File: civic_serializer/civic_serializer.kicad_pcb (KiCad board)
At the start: 2 copper layers, 65 x 30 mm, 5 parts, among them J1 GPIO

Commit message: - done some of the layout
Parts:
- added C1: 100n, Capacitor_SMD:C_0805_2012Metric_Pad1.18x1.45mm_HandSolder, F.Cu at (58.6, 45.9)
- added C10: 4.7u, Capacitor_SMD:C_0805_2012Metric_Pad1.18x1.45mm_HandSolder, F.Cu at (63.4, 57.9)
- added C11: 100n, Capacitor_SMD:C_0805_2012Metric_Pad1.18x1.45mm_HandSolder, F.Cu at (153.3, 83.7)
- added C12: 100n, Capacitor_SMD:C_0805_2012Metric_Pad1.18x1.45mm_HandSolder, F.Cu at (153.3, 86.5)
- added C13: 10uF, Capacitor_SMD:C_0805_2012Metric_Pad1.18x1.45mm_HandSolder, F.Cu at (68.2, 51.9)
- added C2: 10u, Capacitor_SMD:C_0805_2012Metric_Pad1.18x1.45mm_HandSolder, F.Cu at (58.6, 48.9)
- added C3: 10u, Capacitor_SMD:C_0805_2012Metric_Pad1.18x1.45mm_HandSolder, F.Cu at (58.6, 51.9)
- added C4: 10u, Capacitor_SMD:C_0805_2012Metric_Pad1.18x1.45mm_HandSolder, F.Cu at (58.6, 54.9)
- added C5: 4.7u, Capacitor_SMD:C_0805_2012Metric_Pad1.18x1.45mm_HandSolder, F.Cu at (58.6, 57.9)
- added C6: 4.7u, Capacitor_SMD:C_0805_2012Metric_Pad1.18x1.45mm_HandSolder, F.Cu at (63.4, 45.9)
- added C7: 4.7u, Capacitor_SMD:C_0805_2012Metric_Pad1.18x1.45mm_HandSolder, F.Cu at (63.4, 48.9)
- added C8: 4.7u, Capacitor_SMD:C_0805_2012Metric_Pad1.18x1.45mm_HandSolder, F.Cu at (63.4, 51.9)
- added C9: 4.7u, Capacitor_SMD:C_0805_2012Metric_Pad1.18x1.45mm_HandSolder, F.Cu at (63.4, 54.9)
- added D1: LED, LED_SMD:LED_0805_2012Metric_Pad1.15x1.40mm_HandSolder, F.Cu at (68.1, 61.0)
- added FB1: FerriteBead, Inductor_SMD:L_0805_2012Metric_Pad1.05x1.20mm_HandSolder, F.Cu at (63.2, 60.8)
- added FB2: FerriteBead, Inductor_SMD:L_0805_2012Metric_Pad1.05x1.20mm_HandSolder, F.Cu at (63.2, 63.6)
- added I2C1: Conn_01x02_Socket, Connector_PinSocket_2.54mm:PinSocket_1x02_P2.54mm_Vertical, F.Cu at (144.4, 97.0)
- added IC1: DS90UB925QSQX_NOPB, Footprint_library:QFN50P700X700X80-49N-D, F.Cu at (144.7, 85.6)
- added LVDS1: Conn_01x03_Pin, Connector_JST:JST_NV_B03P-NV_1x03_P5.00mm_Vertical, F.Cu at (159.4, 89.9)
- added R1: 4K7, Resistor_SMD:R_0805_2012Metric_Pad1.20x1.40mm_HandSolder, F.Cu at (53.8, 35.3)
- added R2: 10K, Resistor_SMD:R_0805_2012Metric_Pad1.20x1.40mm_HandSolder, F.Cu at (53.8, 38.3)
- added R3: 4K7, Resistor_SMD:R_0805_2012Metric_Pad1.20x1.40mm_HandSolder, F.Cu at (53.8, 41.2)
- added R4: 4K7, Resistor_SMD:R_0805_2012Metric_Pad1.20x1.40mm_HandSolder, F.Cu at (53.8, 44.2)
- added R5: 4K7, Resistor_SMD:R_0805_2012Metric_Pad1.20x1.40mm_HandSolder, F.Cu at (53.8, 47.1)
- added R6: 100R, Resistor_SMD:R_0805_2012Metric_Pad1.20x1.40mm_HandSolder, F.Cu at (53.8, 50.1)
- added R7: R, Resistor_SMD:R_0805_2012Metric_Pad1.20x1.40mm_HandSolder, F.Cu at (53.8, 53.0)
- added R8: 100R, Resistor_SMD:R_0805_2012Metric_Pad1.20x1.40mm_HandSolder, F.Cu at (53.8, 56.0)
- added R9: R, Resistor_SMD:R_0805_2012Metric_Pad1.20x1.40mm_HandSolder, F.Cu at (53.8, 58.9)
- added RV1: R_Potentiometer_Trim, Potentiometer_THT:Potentiometer_Vishay_T93YA_Vertical, F.Cu at (114.2, 93.4)
- added RV2: R_Potentiometer_Trim, Potentiometer_THT:Potentiometer_Vishay_T93YA_Vertical, F.Cu at (73.7, 54.7)
- added U1: AMS1117-3.3, Package_TO_SOT_SMD:SOT-223-3_TabPin2, F.Cu at (75.5, 62.2)
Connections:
- J1 pad 10: /GPIO15/RXD0 -> G3
- J1 pad 11: /GPIO17 -> G5
- J1 pad 12: /GPIO18/PCM.CLK -> G6
- J1 pad 13: /GPIO27 -> R7
- J1 pad 15: /GPIO22 -> R2
- J1 pad 16: /GPIO23 -> R3
- J1 pad 18: /GPIO24 -> R4
- J1 pad 19: /GPIO10/SPI0.MOSI -> B6
- J1 pad 21: /GPIO9/SPI0.MISO -> B5
- J1 pad 22: /GPIO25 -> R5
- J1 pad 23: /GPIO11/SPI0.SCLK -> B7
- J1 pad 24: /GPIO8/SPI0.CE0 -> B4
- J1 pad 26: /GPIO7/SPI0.CE1 -> B3
- J1 pad 27: /ID_SDA -> PCLK
- J1 pad 28: /ID_SCL -> DE
- J1 pad 29: /GPIO5 -> B1
- J1 pad 3: /GPIO2/SDA1 -> VSYNC
- J1 pad 31: /GPIO6 -> B2
- J1 pad 32: /GPIO12/PWM0 -> G0
- J1 pad 33: /GPIO13/PWM1 -> G1
- J1 pad 35: /GPIO19/PCM.FS -> G7
- J1 pad 36: /GPIO16 -> G4
- J1 pad 37: /GPIO26 -> R6
- J1 pad 38: /GPIO20/PCM.DIN -> R0
- J1 pad 40: /GPIO21/PCM.DOUT -> R1
- J1 pad 5: /GPIO3/SCL1 -> HSYNC
- J1 pad 7: /GPIO4/GPCLK0 -> B0
- J1 pad 8: /GPIO14/TXD0 -> G2
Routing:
- net B7: track 0.00 -> 41.0 mm, vias 0 -> 5
- net VSYNC: track 0.00 -> 40.3 mm
- net HSYNC: track 0.00 -> 36.9 mm
- net G3: track 0.00 -> 36.9 mm
- net G6: track 0.00 -> 31.9 mm, vias 0 -> 1
- net G2: track 0.00 -> 31.3 mm
- net B6: track 0.00 -> 30.1 mm, vias 0 -> 3
- net R3: track 0.00 -> 29.6 mm
- net B5: track 0.00 -> 27.9 mm, vias 0 -> 4
- net R2: track 0.00 -> 25.7 mm
- net R4: track 0.00 -> 25.6 mm, vias 0 -> 1
- net B4: track 0.00 -> 25.5 mm, vias 0 -> 2
- net G4: track 0.00 -> 25.5 mm, vias 0 -> 1
- net G7: track 0.00 -> 25.5 mm, vias 0 -> 2
- net B3: track 0.00 -> 25.3 mm, vias 0 -> 2
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- added copper zone on B.Cu, net GND
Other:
- board text removed: "Extend PCB edge 0.5mm if using SMT header"
- board text removed: "PoE"

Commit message: - layout finished
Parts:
- removed D1: LED, LED_SMD:LED_0805_2012Metric_Pad1.15x1.40mm_HandSolder
- removed RV1, RV2: R_Potentiometer_Trim, Potentiometer_THT:Potentiometer_Vishay_T93YA_Vertical
- added 5V1: LED, LED_SMD:LED_0805_2012Metric_Pad1.15x1.40mm_HandSolder, F.Cu at (103.3, 79.4)
- added IDX1: R_Potentiometer_Trim, Potentiometer_THT:Potentiometer_Vishay_T93YA_Vertical, F.Cu at (117.9, 94.9)
- added IDX2: TestPoint, Connector_PinSocket_2.54mm:PinSocket_1x01_P2.54mm_Vertical, F.Cu at (111.4, 97.1)
- added MDE1: TestPoint, Connector_PinSocket_2.54mm:PinSocket_1x01_P2.54mm_Vertical, F.Cu at (132.9, 97.1)
- added MD_SEL1: R_Potentiometer_Trim, Potentiometer_THT:Potentiometer_Vishay_T93YA_Vertical, F.Cu at (126.3, 95.0)
- C1, C13: footprint Capacitor_SMD:C_0805_2012Metric_Pad1.18x1.45mm_HandSolder -> Capacitor_SMD:C_0603_1608Metric_Pad1.08x0.95mm_HandSolder; moved to B.Cu
- C10, C11, C12, C5, C6, C7, C8, C9: footprint Capacitor_SMD:C_0805_2012Metric_Pad1.18x1.45mm_HandSolder -> Capacitor_SMD:C_0603_1608Metric_Pad1.08x0.95mm_HandSolder
- C2, C3, C4: moved to B.Cu
- FB1, FB2: footprint Inductor_SMD:L_0805_2012Metric_Pad1.05x1.20mm_HandSolder -> Inductor_SMD:L_0603_1608Metric_Pad1.05x0.95mm_HandSolder; moved to B.Cu
- R2, R3, R4, R5: footprint Resistor_SMD:R_0805_2012Metric_Pad1.20x1.40mm_HandSolder -> Resistor_SMD:R_0603_1608Metric_Pad0.98x0.95mm_HandSolder; moved to B.Cu
- R6, R7, R8, R9: footprint Resistor_SMD:R_0805_2012Metric_Pad1.20x1.40mm_HandSolder -> Resistor_SMD:R_0603_1608Metric_Pad0.98x0.95mm_HandSolder
- moved R4 109.4 mm to (149.0, 98.0)
- moved R2 107.8 mm to (150.0, 86.9)
- moved R5 107.2 mm to (149.0, 96.4)
- moved C1 98.3 mm to (149.3, 83.9), turned to -90 degrees
- moved C7 95.7 mm to (149.9, 89.7)
- moved C8 94.9 mm to (149.0, 92.9)
- moved R3 94.7 mm to (139.8, 81.0), turned to 180 degrees
- moved C9 94.4 mm to (149.0, 94.5)
- moved C10 92.3 mm to (149.4, 91.3)
- moved C13 89.7 mm to (150.0, 88.6)
- moved C6 88.4 mm to (145.0, 79.9), turned to 180 degrees
- moved C5 83.7 mm to (139.1, 81.0)
- moved FB2 83.7 mm to (145.5, 78.9)
- moved FB1 78.7 mm to (139.8, 78.9)
- moved R7 78.5 mm to (125.4, 85.3), turned to 90 degrees
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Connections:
- net Net-(IC1-DOUT+) renamed DOUT+
- net Net-(IC1-DOUT-) renamed DOUT-
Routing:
- net VDDIO: track 0.00 -> 97.9 mm, vias 0 -> 6
- net GND: track 0.00 -> 81.0 mm, vias 8 -> 10
- net 3V3: track 0.00 -> 50.2 mm, vias 0 -> 2
- net MODE_SEL: track 0.00 -> 47.2 mm, vias 0 -> 1
- net DE: track 0.63 -> 44.9 mm, vias 0 -> 4
- net IDX: track 0.00 -> 43.7 mm, vias 0 -> 2
- net B0: track 0.00 -> 29.1 mm, vias 0 -> 1
- net +3V3: track 0.00 -> 25.5 mm, vias 0 -> 2
- net PCLK: track 1.48 -> 26.9 mm
- net +5V: track 0.00 -> 14.0 mm, vias 0 -> 1
- net VDD33: track 0.00 -> 10.1 mm, vias 0 -> 2
- net B2: track 21.5 -> 30.5 mm
- net G3: track 36.9 -> 28.0 mm, vias 0 -> 1
- net CAPL12: track 0.00 -> 8.43 mm, vias 0 -> 2
- net G7: track 25.5 -> 32.9 mm, vias 2 -> 3
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- added copper zone on F.Cu, net GND

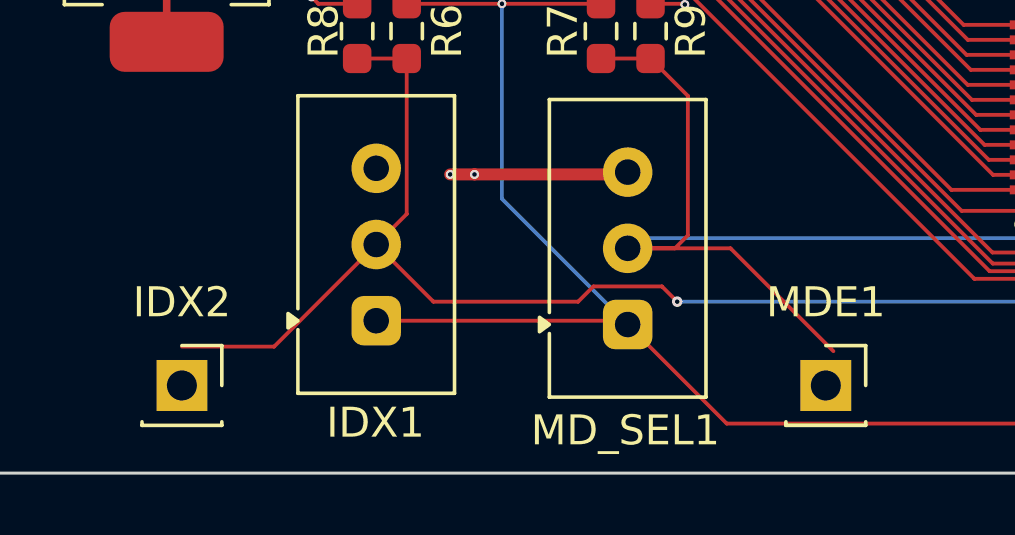
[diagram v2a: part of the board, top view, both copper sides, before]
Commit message: - fixed drc error
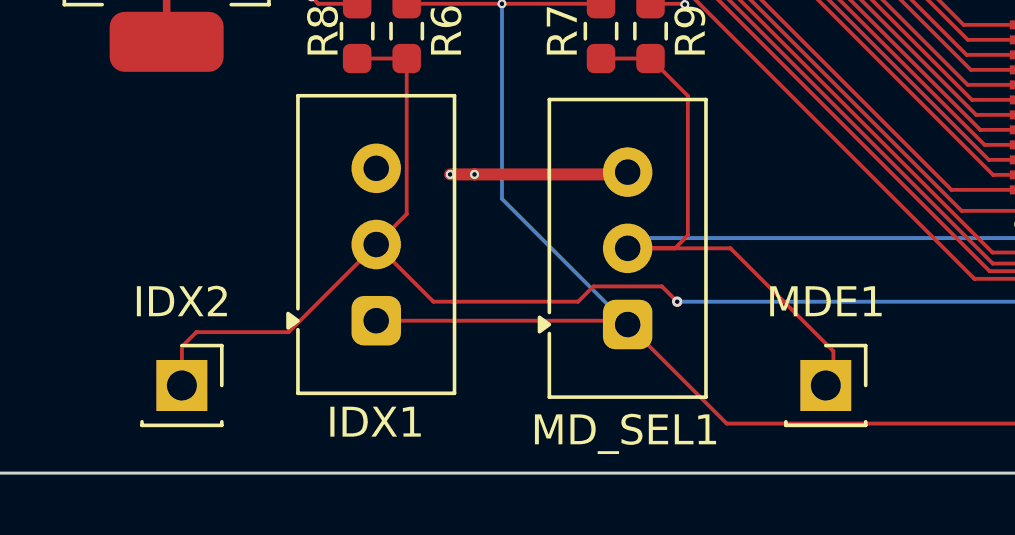
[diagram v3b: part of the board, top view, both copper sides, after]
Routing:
- net IDX: track 43.7 -> 45.0 mm
- net MODE_SEL: track 47.2 -> 48.4 mm
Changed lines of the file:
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@@
 		)
 		(fp_text user "${REFERENCE}"
-			(at 0 0 360)
+			(at 0 0 0)
 			(layer "F.Fab")
 			(effects
@@
 		(tags "capacitor handsolder")
 		(property "Reference" "C6"
-			(at 0 -1.43 360)
+			(at 0 -1.43 0)
 			(layer "F.SilkS")
 			(effects
@@
 		)
 		(property "Value" "4.7u"
-			(at 0 1.43 360)
+			(at 0 1.43 0)
 			(layer "F.Fab")
 			(effects
@@
 		)
 		(fp_text user "${REFERENCE}"
-			(at 0 0 360)
+			(at 0 0 0)
 			(layer "F.Fab")
 			(effects
@@
 		(tags "capacitor handsolder")
 		(property "Reference" "C8"
-			(at 2.54 -0.0508 360)
+			(at 2.54 -0.0508 0)
 			(layer "F.SilkS")
 			(effects
@@
 		)
 		(property "Value" "4.7u"
-			(at 0 1.43 360)
+			(at 0 1.43 0)
 			(layer "F.Fab")
 			(effects
@@
 		)
 		(fp_text user "${REFERENCE}"
-			(at 0 0 360)
+			(at 0 0 0)
 			(layer "F.Fab")
 			(effects
@@
 		(tags "resistor handsolder")
 		(property "Reference" "R5"
-			(at 2.7432 -0.0508 360)
+			(at 2.7432 -0.0508 0)
 			(layer "B.SilkS")
 			(effects
@@
 		)
 		(property "Value" "4K7"
-			(at 0 -1.43 360)
+			(at 0 -1.43 0)
 			(layer "B.Fab")
 			(effects
@@
 		)
 		(fp_text user "${REFERENCE}"
-			(at 0 0 360)
+			(at 0 0 0)
 			(layer "B.Fab")
 			(effects
@@
 		(tags "resistor handsolder")
 		(property "Reference" "R2"
-			(at 2.4384 -0.0762 360)
+			(at 2.4384 -0.0762 0)
 			(layer "B.SilkS")
 			(effects
@@
 		)
 		(property "Value" "10K"
-			(at 0 -1.43 360)
+			(at 0 -1.43 0)
 			(layer "B.Fab")
 			(effects
@@
 		)
 		(fp_text user "${REFERENCE}"
-			(at 0 0 360)
+			(at 0 0 0)
 			(layer "B.Fab")
 			(effects
@@
 		(tags "resistor handsolder")
 		(property "Reference" "R4"
-			(at 2.7197 0 360)
+			(at 2.7197 0 0)
 			(layer "B.SilkS")
 			(effects
@@
 		)
 		(property "Value" "4K7"
-			(at 0 -1.43 360)
+			(at 0 -1.43 0)
 			(layer "B.Fab")
 			(effects
@@
 		)
 		(fp_text user "${REFERENCE}"
-			(at 0 0 360)
+			(at 0 0 0)
 			(layer "B.Fab")
 			(effects
@@
 		(tags "capacitor handsolder")
 		(property "Reference" "C13"
-			(at 2.9464 0.1016 360)
+			(at 2.9464 0.1016 0)
 			(layer "B.SilkS")
 			(effects
@@
 		)
 		(property "Value" "10uF"
-			(at 0 -1.43 360)
+			(at 0 -1.43 0)
 			(layer "B.Fab")
 			(effects
@@
 		)
 		(fp_text user "${REFERENCE}"
-			(at 0 0 360)
+			(at 0 0 0)
 			(layer "B.Fab")
 			(effects
@@
 	)
 	(segment
+		(start 133.147 96.825)
+		(end 132.893 97.079)
+		(width 0.127)
+		(layer "F.Cu")
+		(net 18)
+	)
+	(segment
+		(start 133.147 95.936)
+		(end 133.147 96.825)
+		(width 0.127)
+		(layer "F.Cu")
+		(net 18)
+	)
+	(segment
 		(start 147.454 85.058)
 		(end 147.498 85.014)
@@
 	)
 	(segment
+		(start 114.986 95.301)
+		(end 117.907 92.38)
+		(width 0.127)
+		(layer "F.Cu")
+		(net 27)
+	)
+	(segment
 		(start 118.923 91.364)
 		(end 117.907 92.38)
@@
 	)
 	(segment
-		(start 117.272 86.1805)
-		(end 118.923 86.1805)
+		(start 111.9126 95.301)
+		(end 114.986 95.301)
 		(width 0.127)
 		(layer "F.Cu")
@@
 	)
 	(segment
-		(start 140.005 94.285)
-		(end 140.226 94.285)
+		(start 117.272 86.1805)
+		(end 118.923 86.1805)
 		(width 0.127)
 		(layer "F.Cu")
@@
 	)
 	(segment
-		(start 114.5034 95.7836)
-		(end 117.907 92.38)
+		(start 140.005 94.285)
+		(end 140.226 94.285)
 		(width 0.127)
 		(layer "F.Cu")
@@
 	)
 	(segment
+		(start 111.43 95.7836)
+		(end 111.43 97.079)
+		(width 0.127)
+		(layer "F.Cu")
+		(net 27)
+	)
+	(segment
 		(start 142.676 91.835)
 		(end 142.676 91.258)
@@
 	(segment
 		(start 111.43 95.7836)
-		(end 114.5034 95.7836)
+		(end 111.9126 95.301)
 		(width 0.127)
 		(layer "F.Cu")
